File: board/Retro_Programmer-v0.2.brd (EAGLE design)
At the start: 45 x 45 mm, 48 parts, among them IC1 74LVC125A, K1 61301511821, K2 61301511821, P1 POWERSUPPLY_DC21MMX, Q1 BC857CSMD, Q2 BC847, SW1 SPUSH, SW2 SPUSH, SW3 SPUSH, SW4 SLIDE_WAY4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

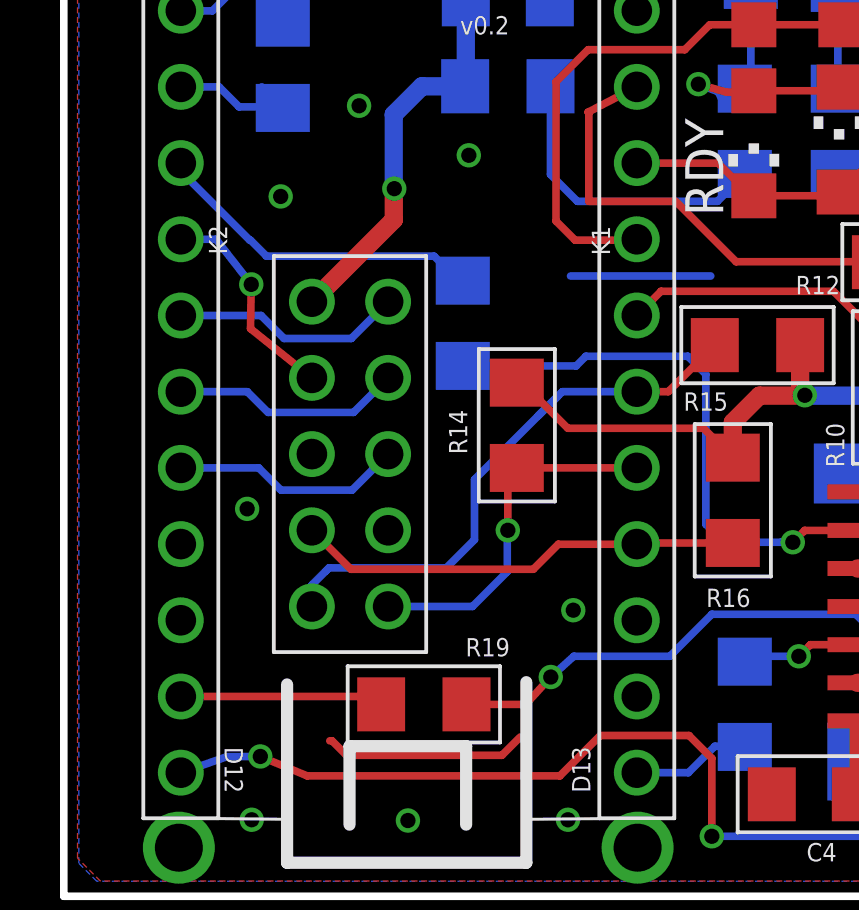
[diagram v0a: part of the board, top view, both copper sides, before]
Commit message: Mirrored ICSP
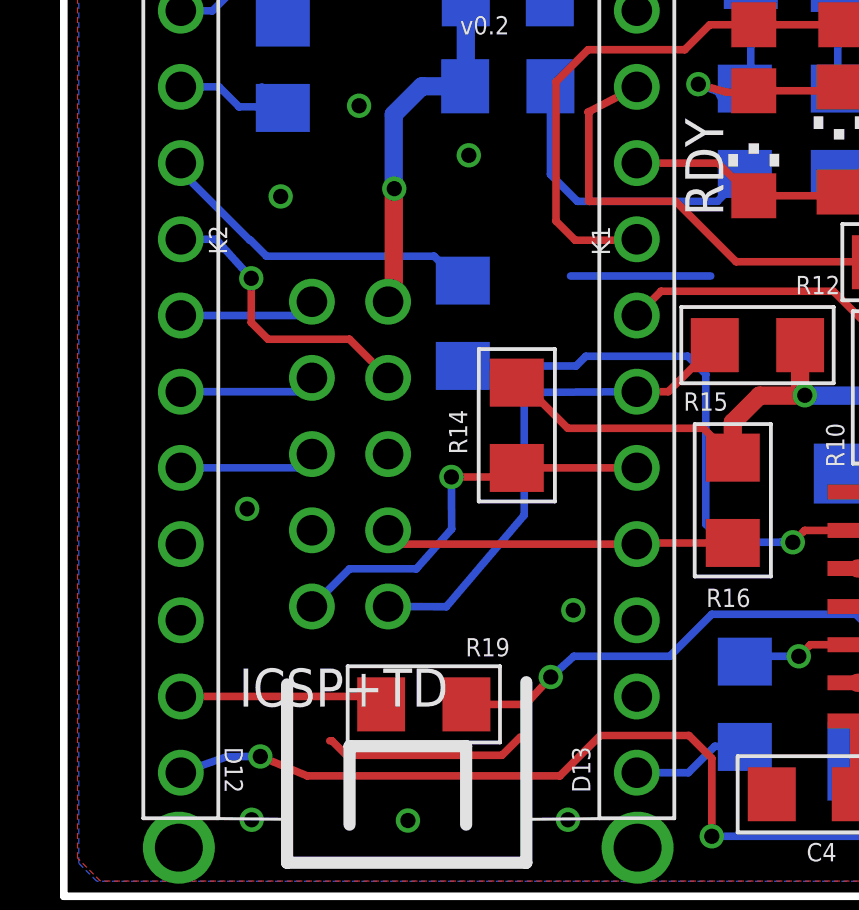
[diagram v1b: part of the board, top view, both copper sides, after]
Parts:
- flipped ICSP+TD to the bottom
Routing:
- net A0: track 14.9 -> 11.7 mm
- net D6: track 7.74 -> 4.56 mm
- net D8: track 7.72 -> 4.56 mm
- net D7: track 7.67 -> 4.56 mm
- net D5: track 7.18 -> 9.73 mm
- net A2: track 19.6 -> 17.0 mm
- net A1: track 12.0 -> 13.8 mm
- net D3ENB: track 18.1 -> 17.1 mm
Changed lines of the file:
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@@
 <layers>
 <layer number="1" name="Top" color="4" fill="1" visible="yes" active="yes"/>
-<layer number="16" name="Bottom" color="1" fill="1" visible="no" active="yes"/>
+<layer number="16" name="Bottom" color="1" fill="1" visible="yes" active="yes"/>
 <layer number="17" name="Pads" color="2" fill="1" visible="yes" active="yes"/>
 <layer number="18" name="Vias" color="2" fill="1" visible="yes" active="yes"/>
 <layer number="19" name="Unrouted" color="6" fill="1" visible="yes" active="yes"/>
 <layer number="20" name="Dimension" color="15" fill="1" visible="yes" active="yes"/>
-<layer number="21" name="tPlace" color="7" fill="1" visible="yes" active="yes"/>
+<layer number="21" name="tPlace" color="7" fill="1" visible="no" active="yes"/>
 <layer number="22" name="bPlace" color="7" fill="1" visible="yes" active="yes"/>
-<layer number="23" name="tOrigins" color="15" fill="1" visible="yes" active="yes"/>
+<layer number="23" name="tOrigins" color="15" fill="1" visible="no" active="yes"/>
 <layer number="24" name="bOrigins" color="15" fill="1" visible="yes" active="yes"/>
-<layer number="25" name="tNames" color="7" fill="1" visible="yes" active="yes"/>
+<layer number="25" name="tNames" color="7" fill="1" visible="no" active="yes"/>
 <layer number="26" name="bNames" color="7" fill="1" visible="yes" active="yes"/>
 <layer number="27" name="tValues" color="7" fill="1" visible="no" active="yes"/>
@@
 <attribute name="VALUE" x="28.6554" y="15.3564" size="0.6096" layer="27" rot="R180"/>
 </element>
-<element name="ICSP+TD" library="Wuerth_Elektronik_Board_to_Board" package="61301021821" value="61301021821" x="9.54" y="14.74" smashed="yes" rot="R90">
-<attribute name="NAME" x="13.2417" y="6.3214" size="1.27" layer="26" rot="MR0"/>
-<attribute name="VALUE" x="18.8178" y="3.5528" size="1.27" layer="27" rot="R90"/>
+<element name="ICSP+TD" library="Wuerth_Elektronik_Board_to_Board" package="61301021821" value="61301021821" x="9.54" y="14.74" smashed="yes" rot="MR90">
+<attribute name="NAME" x="5.8383" y="6.3214" size="1.27" layer="25"/>
+<attribute name="VALUE" x="0.2622" y="3.5528" size="1.27" layer="28" rot="MR90"/>
 </element>
 <element name="RDY" library="led" package="CHIPLED_1206" value="YEL" x="23" y="25.1" smashed="yes" rot="R180">
@@
 <contactref element="ICSP+TD" pad="1"/>
 <contactref element="K1" pad="10"/>
-<wire x1="15.8" y1="16.0032" x2="16.4592" y2="16.6624" width="0.254" layer="16"/>
-<wire x1="16.4592" y1="16.6624" x2="16.6168" y2="16.82" width="0.254" layer="16"/>
 <wire x1="19.1" y1="16.82" x2="20.1488" y2="16.82" width="0.254" layer="1"/>
 <wire x1="20.1488" y1="16.82" x2="21.7002" y2="18.3714" width="0.254" layer="1"/>
-<wire x1="19.1" y1="16.82" x2="16.6168" y2="16.82" width="0.254" layer="16"/>
-<wire x1="8.27" y1="9.66" x2="8.27" y2="10.3782" width="0.254" layer="16"/>
-<wire x1="8.27" y1="10.3782" x2="8.7376" y2="10.8458" width="0.254" layer="16"/>
-<wire x1="8.7376" y1="10.8458" x2="8.8392" y2="10.9474" width="0.254" layer="16"/>
-<wire x1="8.8392" y1="10.9474" x2="12.7508" y2="10.9474" width="0.254" layer="16"/>
-<wire x1="12.7508" y1="10.9474" x2="13.6906" y2="11.8872" width="0.254" layer="16"/>
-<wire x1="13.6906" y1="11.8872" x2="13.6906" y2="13.8938" width="0.254" layer="16"/>
-<wire x1="13.6906" y1="13.8938" x2="16.4592" y2="16.6624" width="0.254" layer="16"/>
+<wire x1="19.1" y1="16.82" x2="15.3468" y2="16.7946" width="0.254" layer="16"/>
+<wire x1="15.3468" y1="16.7946" x2="15.3468" y2="12.7052" width="0.254" layer="16"/>
+<wire x1="15.3468" y1="12.7052" x2="12.7508" y2="9.652" width="0.254" layer="16"/>
+<wire x1="12.7508" y1="9.652" x2="10.81" y2="9.66" width="0.254" layer="16"/>
 </signal>
 <signal name="A1">
@@
 <contactref element="ICSP+TD" pad="10"/>
 <contactref element="K1" pad="11"/>
-<via x="14.8" y="12.2" extent="1-16" drill="0.508"/>
-<wire x1="14.8" y1="12.2" x2="14.8" y2="13.978" width="0.254" layer="1"/>
+<via x="12.9204" y="13.978" extent="1-16" drill="0.508"/>
+<wire x1="12.9204" y1="13.978" x2="14.8" y2="13.978" width="0.254" layer="1"/>
 <wire x1="14.8" y1="13.978" x2="15.1" y2="14.278" width="0.254" layer="1"/>
 <wire x1="19.1" y1="14.28" x2="15.102" y2="14.28" width="0.254" layer="1"/>
 <wire x1="15.102" y1="14.28" x2="15.1" y2="14.278" width="0.254" layer="1"/>
-<wire x1="10.81" y1="9.66" x2="13.6224" y2="9.66" width="0.254" layer="16"/>
-<wire x1="13.6224" y1="9.66" x2="14.7828" y2="10.8204" width="0.254" layer="16"/>
-<wire x1="14.7828" y1="10.8204" x2="14.7828" y2="12.1828" width="0.254" layer="16"/>
-<wire x1="14.7828" y1="12.1828" x2="14.8" y2="12.2" width="0.254" layer="16"/>
+<wire x1="9.525" y1="10.915" x2="8.27" y2="9.66" width="0.254" layer="16"/>
+<wire x1="9.525" y1="10.915" x2="11.7532" y2="10.915" width="0.254" layer="16"/>
+<wire x1="11.7532" y1="10.915" x2="12.9286" y2="12.2428" width="0.254" layer="16"/>
+<wire x1="12.9286" y1="12.2428" x2="12.9204" y2="13.978" width="0.254" layer="16"/>
 </signal>
 <signal name="A0">
@@
 <contactref element="R16" pad="1"/>
 <contactref element="K1" pad="12"/>
-<wire x1="9.57" y1="10.9" x2="8.27" y2="12.2" width="0.254" layer="1"/>
-<wire x1="9.57" y1="10.9" x2="15.6498" y2="10.9" width="0.254" layer="1"/>
-<wire x1="15.6498" y1="10.9" x2="16.4846" y2="11.7348" width="0.254" layer="1"/>
-<wire x1="16.4846" y1="11.7348" x2="19.0948" y2="11.7348" width="0.254" layer="1"/>
-<wire x1="19.0948" y1="11.7348" x2="19.1" y2="11.74" width="0.254" layer="1"/>
 <wire x1="22.3" y1="11.778" x2="19.138" y2="11.778" width="0.254" layer="1"/>
 <wire x1="19.138" y1="11.778" x2="19.1" y2="11.74" width="0.254" layer="1"/>
+<wire x1="19.1" y1="11.74" x2="11.27" y2="11.74" width="0.254" layer="1"/>
+<wire x1="11.27" y1="11.74" x2="10.81" y2="12.2" width="0.254" layer="1"/>
 </signal>
 <signal name="D13_SD_CLK">
@@
 <contactref element="ICSP+TD" pad="4"/>
 <contactref element="K2" pad="8"/>
-<wire x1="5.0748" y1="21.9" x2="6.2484" y2="20.3962" width="0.254" layer="16"/>
-<via x="6.2484" y="20.3962" extent="1-16" drill="0.508"/>
-<wire x1="6.2484" y1="20.3962" x2="6.223" y2="18.9206" width="0.254" layer="1"/>
-<wire x1="6.223" y1="18.9206" x2="8.27" y2="17.28" width="0.254" layer="1"/>
+<wire x1="5.0748" y1="21.9" x2="6.2484" y2="20.5994" width="0.254" layer="16"/>
+<via x="6.2484" y="20.5994" extent="1-16" drill="0.508"/>
 <wire x1="3.9" y1="21.9" x2="5.0748" y2="21.9" width="0.254" layer="16"/>
+<wire x1="6.2484" y1="20.5994" x2="6.2484" y2="19.1262" width="0.254" layer="1"/>
+<wire x1="6.2484" y1="19.1262" x2="6.8072" y2="18.5674" width="0.254" layer="1"/>
+<wire x1="6.8072" y1="18.5674" x2="9.5226" y2="18.5674" width="0.254" layer="1"/>
+<wire x1="9.5226" y1="18.5674" x2="10.81" y2="17.28" width="0.254" layer="1"/>
 </signal>
 <signal name="D6">
 <contactref element="ICSP+TD" pad="6"/>
 <contactref element="K2" pad="9"/>
-<wire x1="6.5734" y1="19.36" x2="7.3406" y2="18.5928" width="0.254" layer="16"/>
-<wire x1="7.3406" y1="18.5928" x2="9.5828" y2="18.5928" width="0.254" layer="16"/>
-<wire x1="9.5828" y1="18.5928" x2="10.81" y2="19.82" width="0.254" layer="16"/>
-<wire x1="3.9" y1="19.36" x2="6.5734" y2="19.36" width="0.254" layer="16"/>
+<wire x1="3.9" y1="19.36" x2="7.81" y2="19.36" width="0.254" layer="16"/>
+<wire x1="7.81" y1="19.36" x2="8.27" y2="19.82" width="0.254" layer="16"/>
 </signal>
 <signal name="D7">
 <contactref element="ICSP+TD" pad="7"/>
 <contactref element="K2" pad="10"/>
-<wire x1="6.1162" y1="16.82" x2="6.8072" y2="16.129" width="0.254" layer="16"/>
-<wire x1="6.8072" y1="16.129" x2="9.659" y2="16.129" width="0.254" layer="16"/>
-<wire x1="9.659" y1="16.129" x2="10.81" y2="17.28" width="0.254" layer="16"/>
-<wire x1="3.9" y1="16.82" x2="6.1162" y2="16.82" width="0.254" layer="16"/>
+<wire x1="3.9" y1="16.82" x2="7.81" y2="16.82" width="0.254" layer="16"/>
+<wire x1="7.81" y1="16.82" x2="8.27" y2="17.28" width="0.254" layer="16"/>
 </signal>
 <signal name="D8">
 <contactref element="ICSP+TD" pad="8"/>
 <contactref element="K2" pad="11"/>
-<wire x1="6.4972" y1="14.28" x2="7.239" y2="13.5382" width="0.254" layer="16"/>
-<wire x1="7.239" y1="13.5382" x2="9.6082" y2="13.5382" width="0.254" layer="16"/>
-<wire x1="9.6082" y1="13.5382" x2="10.81" y2="14.74" width="0.254" layer="16"/>
-<wire x1="3.9" y1="14.28" x2="6.4972" y2="14.28" width="0.254" layer="16"/>
+<wire x1="3.9" y1="14.28" x2="7.81" y2="14.28" width="0.254" layer="16"/>
+<wire x1="7.81" y1="14.28" x2="8.27" y2="14.74" width="0.254" layer="16"/>
 </signal>
 <signal name="D11_SD_MOSI">
@@
 <wire x1="10.9982" y1="23.6052" x2="11.016" y2="23.5874" width="0.254" layer="16"/>
 <wire x1="10.9998" y1="23.5712" x2="11.016" y2="23.5874" width="0.254" layer="1"/>
-<wire x1="10.9998" y1="23.5712" x2="10.9998" y2="22.5498" width="0.6096" layer="1"/>
-<wire x1="10.9998" y1="22.5498" x2="8.27" y2="19.82" width="0.6096" layer="1"/>
+<wire x1="10.9998" y1="23.5712" x2="10.9998" y2="20.0098" width="0.6096" layer="1"/>
+<wire x1="10.9998" y1="20.0098" x2="10.81" y2="19.82" width="0.6096" layer="1"/>
 </signal>
 <signal name="SD_CLK">

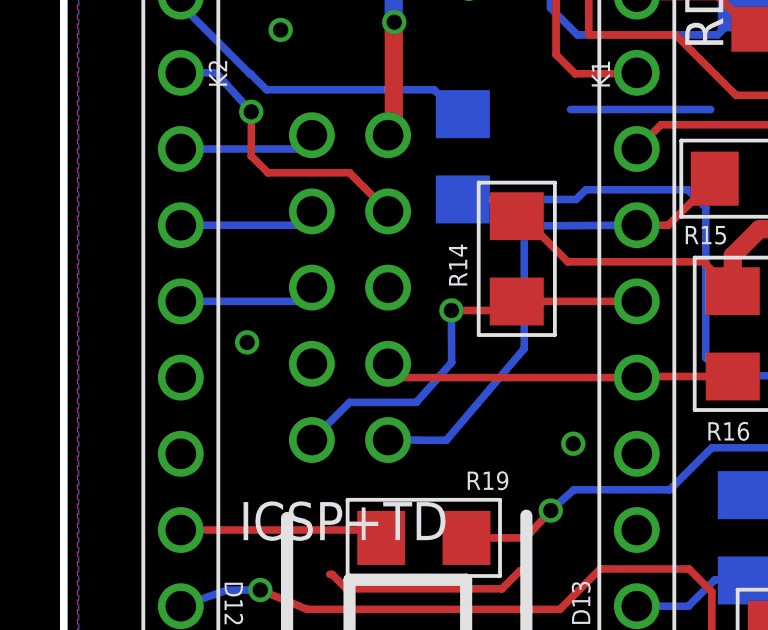
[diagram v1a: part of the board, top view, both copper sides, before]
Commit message: Fixed ground connection to ICSP
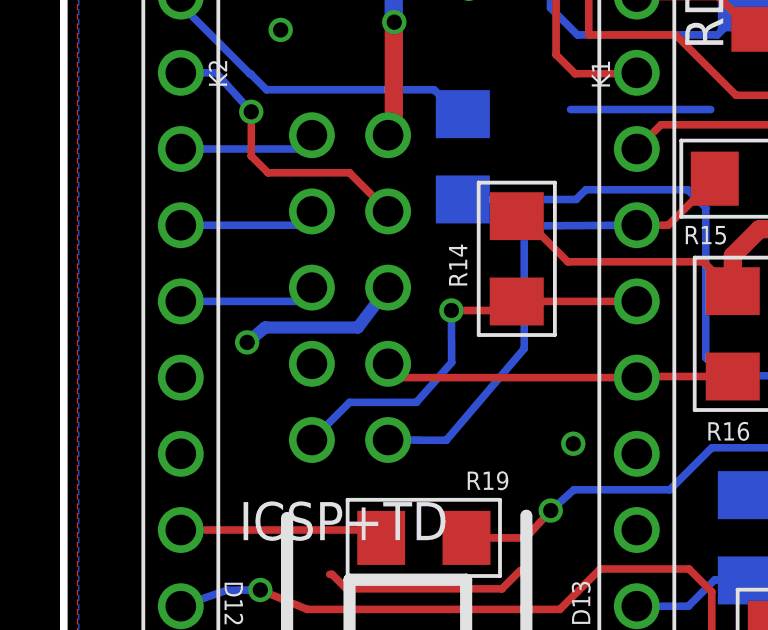
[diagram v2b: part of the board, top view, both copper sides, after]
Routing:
- net GND: track 59.8 -> 65.4 mm
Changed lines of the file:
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@@
 <layer number="19" name="Unrouted" color="6" fill="1" visible="yes" active="yes"/>
 <layer number="20" name="Dimension" color="15" fill="1" visible="yes" active="yes"/>
-<layer number="21" name="tPlace" color="7" fill="1" visible="no" active="yes"/>
-<layer number="22" name="bPlace" color="7" fill="1" visible="yes" active="yes"/>
-<layer number="23" name="tOrigins" color="15" fill="1" visible="no" active="yes"/>
-<layer number="24" name="bOrigins" color="15" fill="1" visible="yes" active="yes"/>
-<layer number="25" name="tNames" color="7" fill="1" visible="no" active="yes"/>
-<layer number="26" name="bNames" color="7" fill="1" visible="yes" active="yes"/>
+<layer number="21" name="tPlace" color="7" fill="1" visible="yes" active="yes"/>
+<layer number="22" name="bPlace" color="7" fill="1" visible="no" active="yes"/>
+<layer number="23" name="tOrigins" color="15" fill="1" visible="yes" active="yes"/>
+<layer number="24" name="bOrigins" color="15" fill="1" visible="no" active="yes"/>
+<layer number="25" name="tNames" color="7" fill="1" visible="yes" active="yes"/>
+<layer number="26" name="bNames" color="7" fill="1" visible="no" active="yes"/>
 <layer number="27" name="tValues" color="7" fill="1" visible="no" active="yes"/>
 <layer number="28" name="bValues" color="7" fill="1" visible="no" active="yes"/>
@@
 <wire x1="24.9936" y1="41.275" x2="24.9936" y2="38.608" width="1.4224" layer="1"/>
 <wire x1="30.1244" y1="41.402" x2="27.1018" y2="41.402" width="1.4224" layer="1"/>
+<wire x1="6.1114" y1="12.914" x2="6.7102" y2="13.4112" width="0.4064" layer="16"/>
+<wire x1="6.7102" y1="13.4112" x2="9.8044" y2="13.4112" width="0.4064" layer="16"/>
+<wire x1="9.8044" y1="13.4112" x2="10.81" y2="14.74" width="0.4064" layer="16"/>
 </signal>
 <signal name="+5V">
